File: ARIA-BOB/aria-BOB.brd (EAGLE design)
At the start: 100 x 80 mm, 14 parts

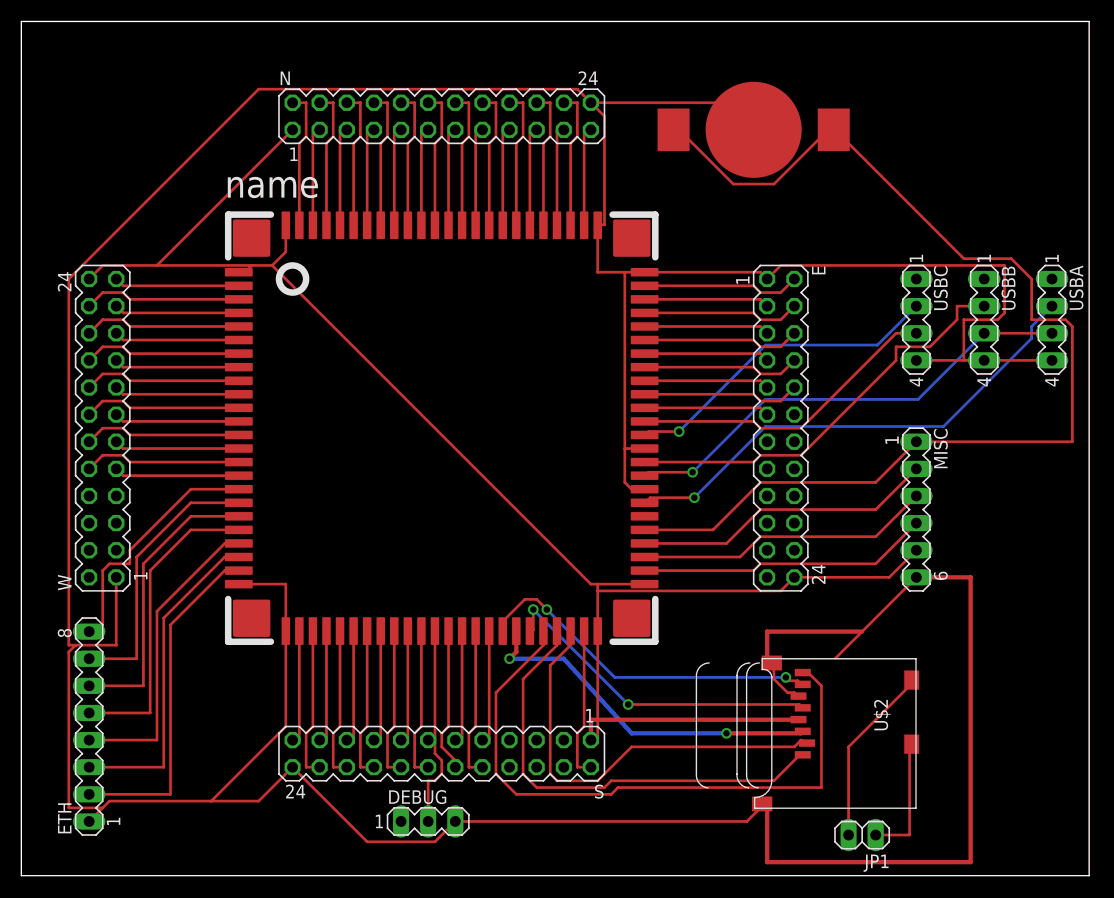
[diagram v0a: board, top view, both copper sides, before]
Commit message: usb wires longer, ground plane, vdd trace wider
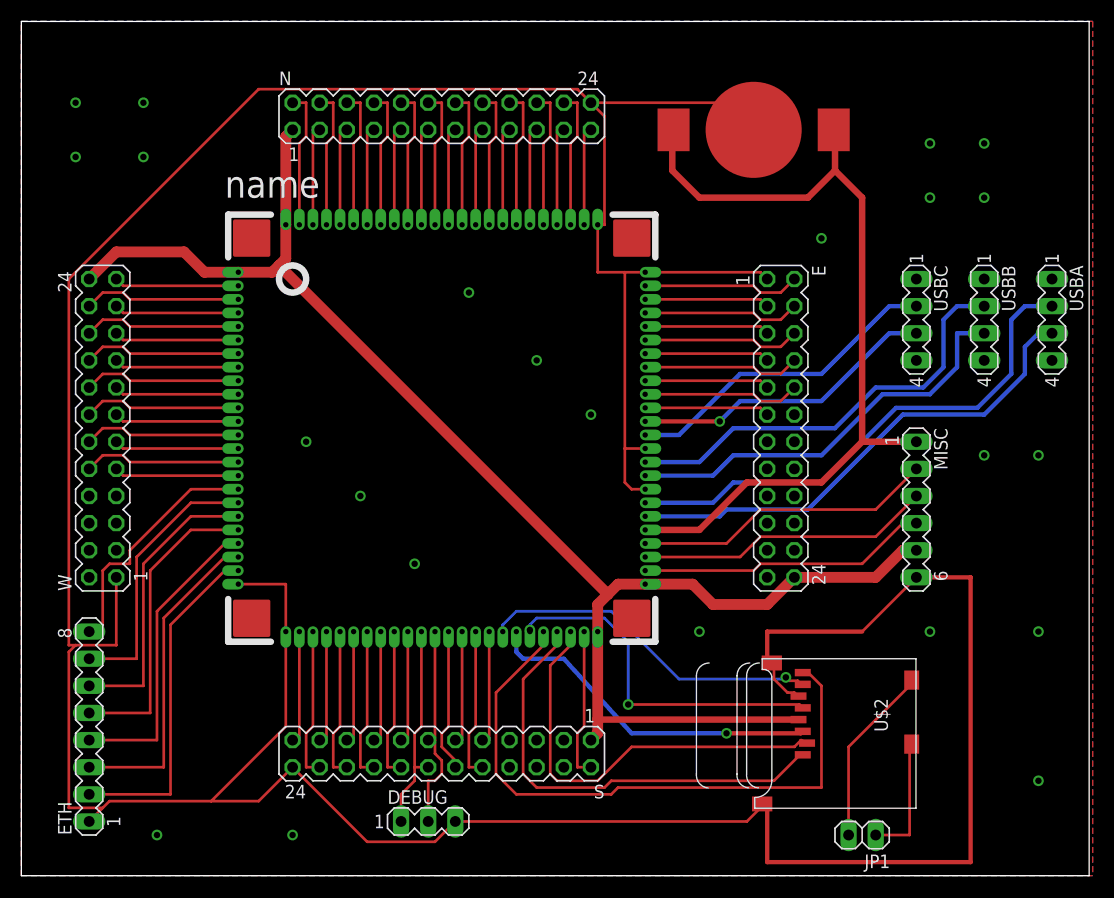
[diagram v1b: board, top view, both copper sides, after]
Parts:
- U$1: value ARIA -> ARIATHROUGHHOLE; device octanis-beat:ARIA -> octanis-beat:ARIA-TROUGHHOLE
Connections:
- net S14: now also DEBUG.1
- net USBA+: now also USBA.3
- net USBB+: no longer USBA.3
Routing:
- net GND: track 423.5 -> 372.3 mm, vias 0 -> 23
- net USBA+: track 0.00 -> 46.7 mm
- net VBAT: track 105.7 -> 80.3 mm
- net VCC: track 156.6 -> 142.0 mm
- net S14: track 14.3 -> 19.8 mm
- net USBB+: track 43.7 -> 39.1 mm, vias 1 -> 0
- net USBA-: track 46.4 -> 48.7 mm, vias 1 -> 0
- net CK: track 31.4 -> 33.4 mm
- net CDA: track 33.5 -> 32.2 mm, vias 2 -> 1
- net USBB-: track 39.3 -> 40.4 mm
- net DA0: track 33.1 -> 32.2 mm, vias 2 -> 1
- net USBC+: track 29.4 -> 28.8 mm, vias 0 -> 1
- net USBC-: vias 1 -> 0
- added copper zone on layer 1, net GND
- added copper zone on layer 16, net GND

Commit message: SD card footprint aria bob
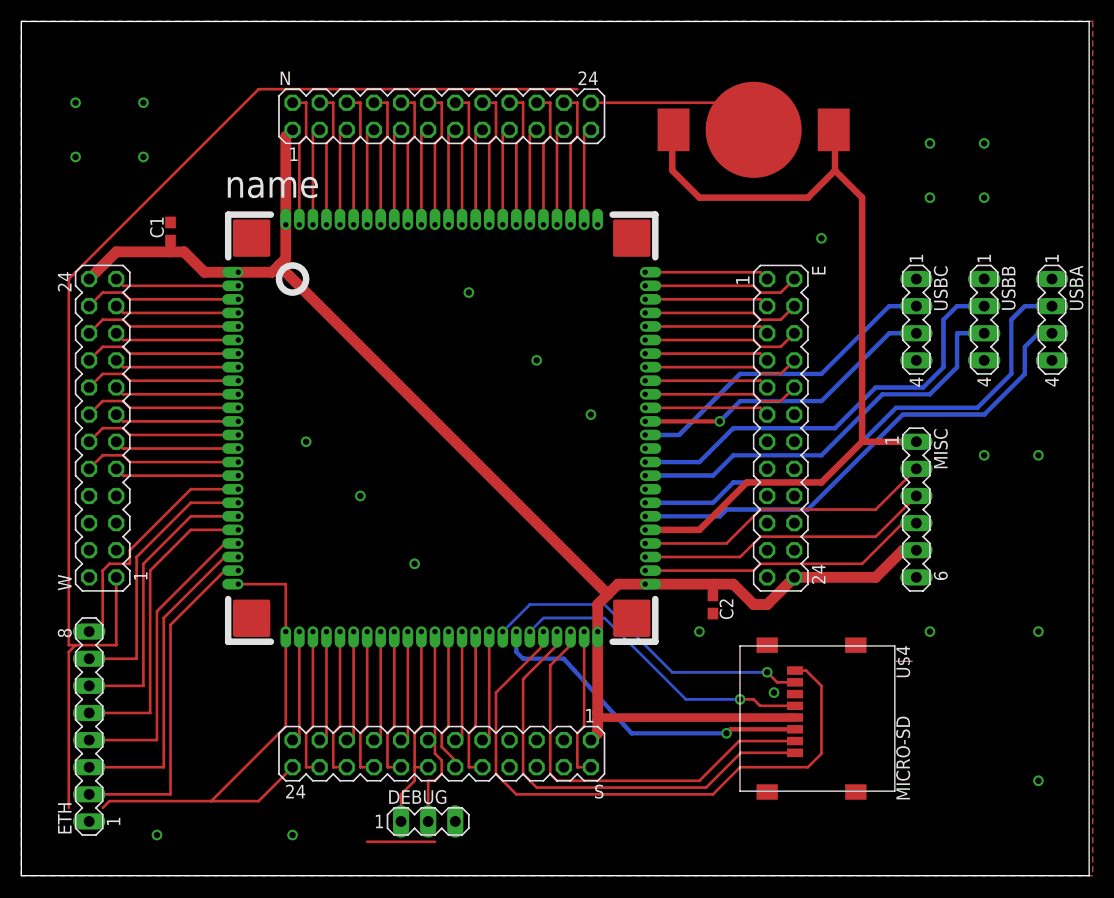
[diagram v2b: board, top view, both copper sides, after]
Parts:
- removed JP1: (no value), pinhead:1X02
- removed U$2: MICROSD, adafruit:MICROSD
- added C1, C2: 100n, rcl:C0603
- added U$4: MICRO-SD, octanis-beat:MISCRO-SD
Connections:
- removed net CD1: JP1.2, U$2.CD1
- removed net CD2: JP1.1, U$2.CD2
- net CDA: now also U$4.CMD; no longer U$2.3
- net CK: now also U$4.CLK; no longer U$2.5
- net DA0: now also U$4.DAT0; no longer U$2.7
- net DA1: now also U$4.DAT1; no longer U$2.8
- net DA2: now also U$4.DAT2; no longer U$2.1
- net DA3: now also U$4.CD/DAT3; no longer U$2.2
- net GND: now also C1.2, C2.2, U$4.G1, U$4.G2, U$4.G3, U$4.G4, U$4.VSS; no longer U$2.6, U$2.MT1, U$2.MT2
- net VCC: now also C1.1, C2.1, U$4.VDD; no longer U$2.4
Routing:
- net GND: track 372.3 -> 196.9 mm, vias 23 -> 24
- net CD1: track 16.9 -> 0.00 mm
- net CD2: track 11.8 -> 0.00 mm
- net CK: track 33.4 -> 28.8 mm, vias 2 -> 1
- net VCC: track 142.0 -> 144.2 mm
- net DA3: track 40.1 -> 38.8 mm
- net DA1: track 58.5 -> 57.4 mm
- net DA2: track 42.7 -> 42.0 mm
- net CDA: track 32.2 -> 31.5 mm
- net DA0: track 32.2 -> 32.9 mm
